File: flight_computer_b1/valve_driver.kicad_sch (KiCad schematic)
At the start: 4 parts, among them U1 IRLML6344TRPBF

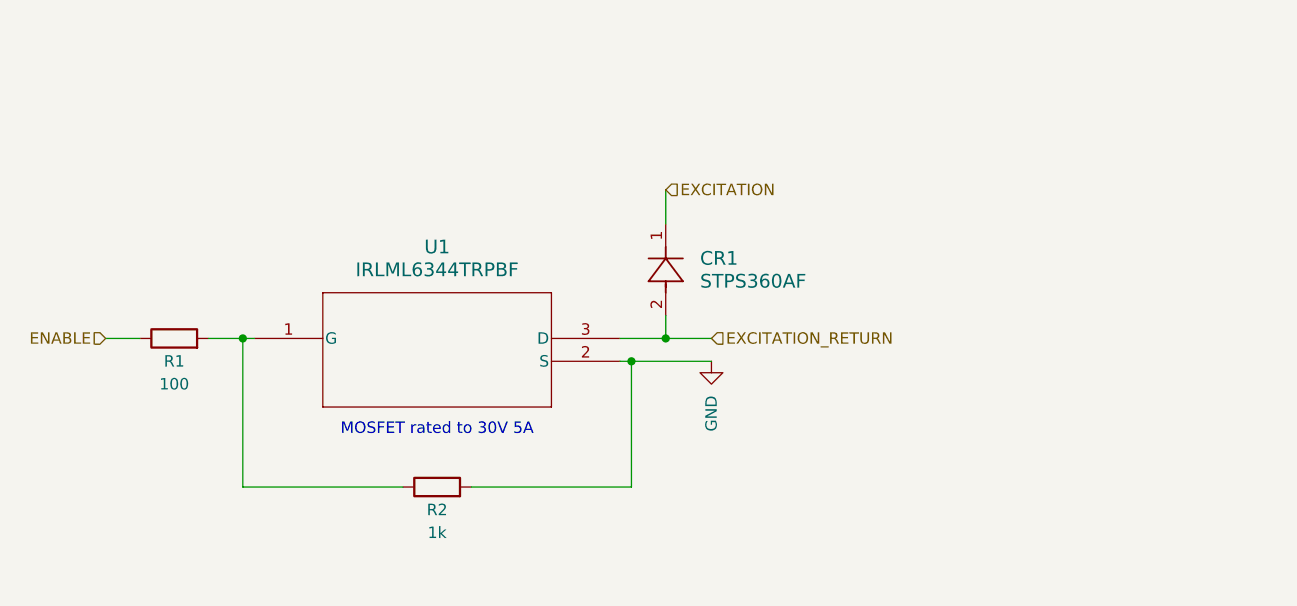
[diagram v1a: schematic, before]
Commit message: flight computer: added mux and voltage sense channels
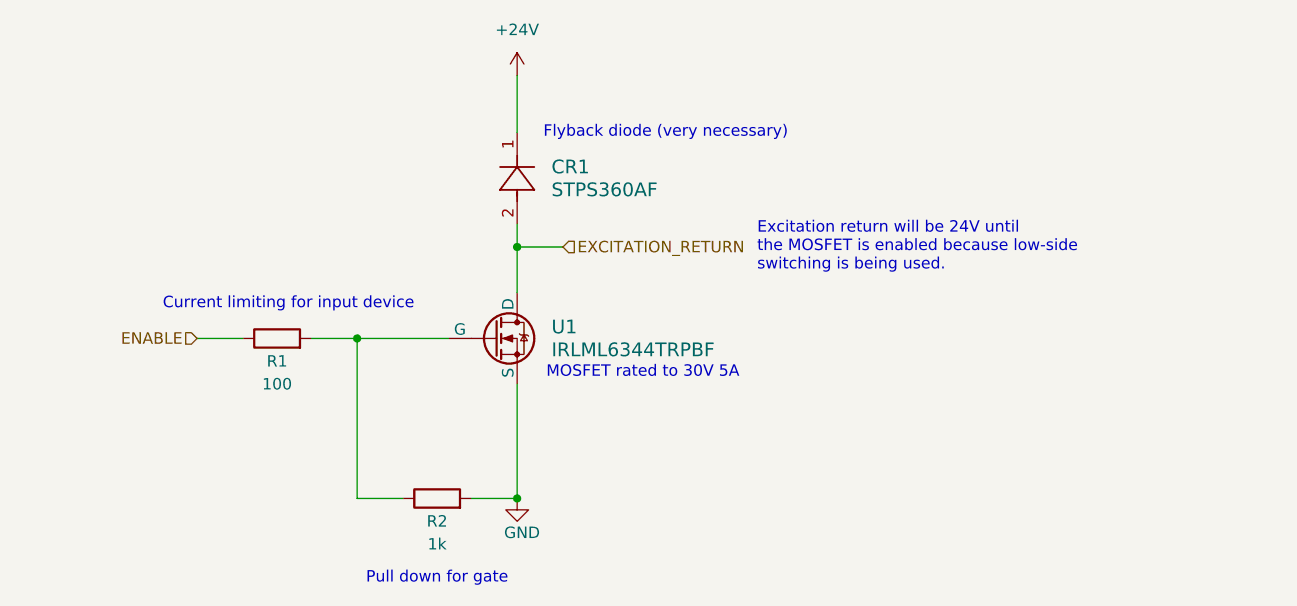
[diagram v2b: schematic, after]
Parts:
- U1: symbol IRLML6344TRPBF:IRLML6344TRPBF -> Simulation_SPICE:NMOS
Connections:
- net EXCITATION_RETURN: now also U1.1 (D); no longer U1.3 (D)
- net GND: now also U1.3 (S); no longer U1.2 (S)
- net at R1.2, R2.1: now also U1.2 (G); no longer U1.1 (G)
- net EXCITATION renamed +24V
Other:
- note added: "Current limiting for input device"
- note added: "Excitation return will be 24V until the MOSFET is enabled because low-side switching is being used."
- note added: "Flyback diode (very necessary)"
- note added: "Pull down for gate"
- company: (none) -> Purdue Space Program Liquids
- moved on the sheet: CR1, R1, R2

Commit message: flight computer: added pyro circuit and digikey part numbers
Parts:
- CR1: DIGIKEY PART N (none) -> 497-16919-1-ND
- R2: DIGIKEY PART N (none) -> YAG1237CT-ND
- U1: DIGIKEY PART N (none) -> IRLML6344TRPBFCT-ND
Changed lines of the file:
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@@
+			)
+		)
+		(property "DIGIKEY PART N" "497-16919-1-ND"
+			(at 147.32 74.93 90)
+			(effects
+				(font
+					(size 1.27 1.27)
+				)
+				(hide yes)
 			)
 		)
@@
 			)
 		)
+		(property "DIGIKEY PART N" ""
+			(at 120.65 87.63 90)
+			(effects
+				(font
+					(size 1.27 1.27)
+				)
+				(hide yes)
+			)
+		)
 		(pin "1"
 		)
@@
 		(property "Description" "Resistor"
 			(at 138.43 105.41 0)
+			(effects
+				(font
+					(size 1.27 1.27)
+				)
+				(hide yes)
+			)
+		)
+		(property "DIGIKEY PART N" "YAG1237CT-ND"
+			(at 138.43 105.41 90)
 			(effects
 				(font
@@
 			(effects
 				(font
+					(size 1.27 1.27)
+				)
+				(hide yes)
+			)
+		)
+		(property "DIGIKEY PART N" "IRLML6344TRPBFCT-ND"
+			(at 144.78 87.63 0)
+			(effects
+				(font

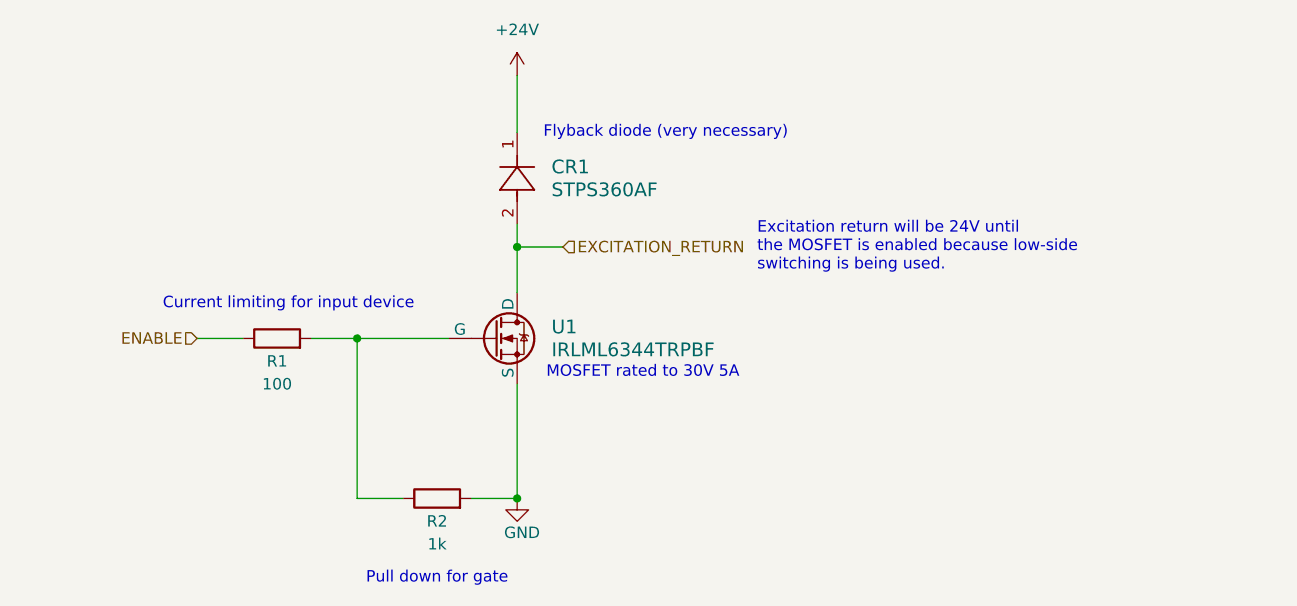
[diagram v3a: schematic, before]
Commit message: flight computer: new ideal diode, small schematic changes
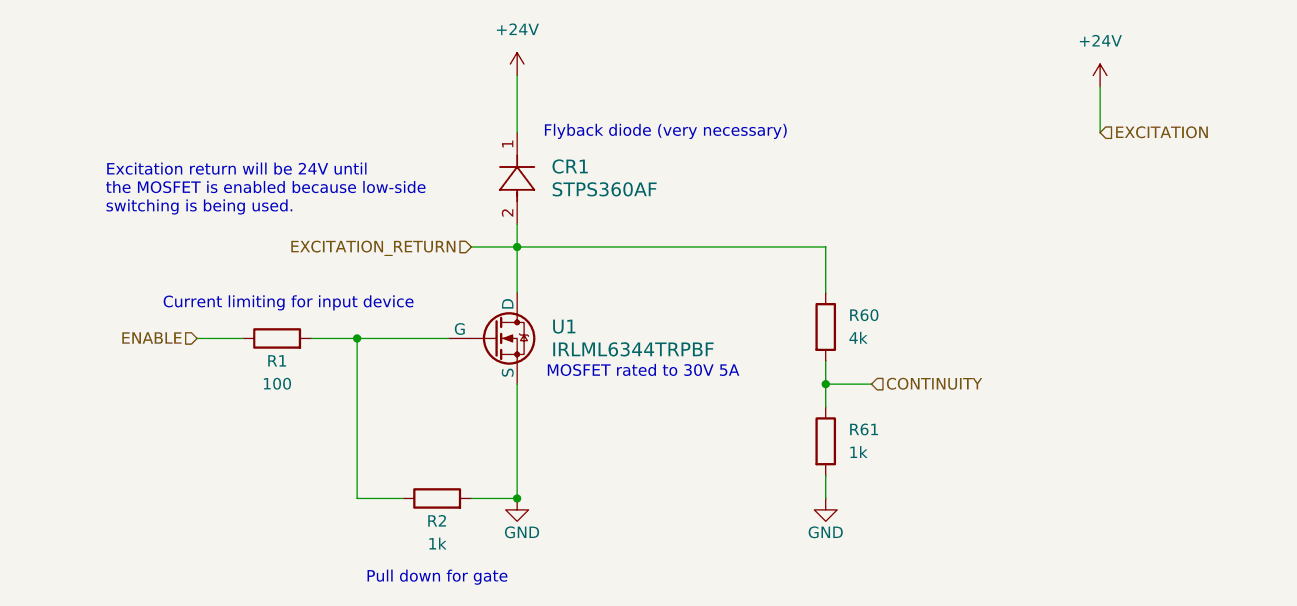
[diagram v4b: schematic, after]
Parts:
- added R60: 4k, Resistor_SMD:R_0603_1608Metric, symbol Device:R
- added R61: 1k, Resistor_SMD:R_0603_1608Metric, symbol Device:R
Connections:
- net EXCITATION_RETURN: now also R60.1
- net GND: now also R61.2
- new net CONTINUITY: R60.2, R61.1

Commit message: flight computer: routing updates
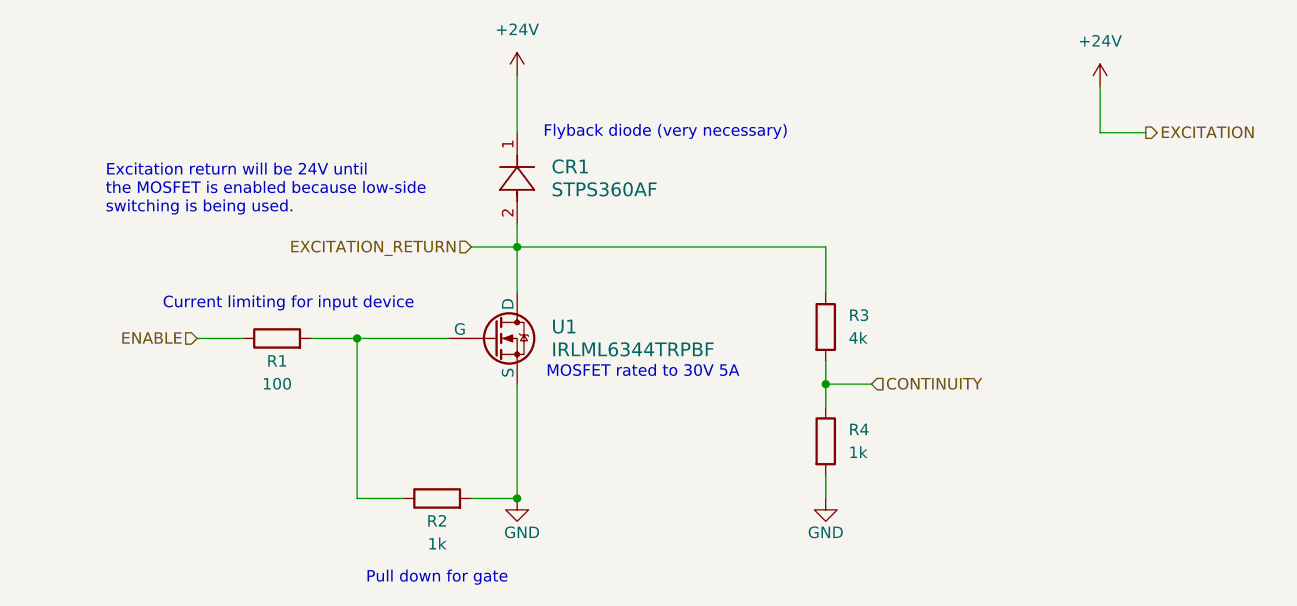
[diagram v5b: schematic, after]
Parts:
- R1: DIGIKEY PART N (none) -> 541-100HCT-ND
- renumbered R60 to R3, R61 to R4
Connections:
- net EXCITATION_RETURN: now also U1.3 (D); no longer U1.1 (D)
- net GND: now also U1.2 (S); no longer U1.3 (S)
- net at R1.2, R2.1: now also U1.1 (G); no longer U1.2 (G)
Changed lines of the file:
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@@
+	(wire
+		(pts
+			(xy 212.09 64.77) (xy 212.09 59.69)
+		)
+		(stroke
+			(width 0)
+			(type default)
+		)
+	)
 	(wire
 		(pts
@@
 	(wire
 		(pts
-			(xy 212.09 64.77) (xy 212.09 59.69)
-		)
-		(stroke
-			(width 0)
-			(type default)
-		)
-	)
-	(wire
-		(pts
 			(xy 181.61 90.17) (xy 181.61 92.71)
 		)
@@
 		(pts
 			(xy 134.62 105.41) (xy 129.54 105.41)
+		)
+		(stroke
+			(width 0)
+			(type default)
+		)
+	)
+	(wire
+		(pts
+			(xy 217.17 64.77) (xy 212.09 64.77)
 		)
 		(stroke
@@
 	)
 	(hierarchical_label "EXCITATION"
-		(shape input)
-		(at 212.09 64.77 0)
+		(shape output)
+		(at 217.17 64.77 0)
 		(effects
 			(font
@@
 			)
 		)
-		(property "DIGIKEY PART N" ""
+		(property "DIGIKEY PART N" "541-100HCT-ND"
 			(at 120.65 87.63 90)
 			(effects
@@
 			(project "flight_computer"
 				(path "/b71a7b79-cdb5-4e38-a72c-0daaa3474f05/299e6e4e-fa99-4a32-b6f8-bfb69183cdb6"
-					(reference "R7")
+					(reference "R13")
 					(unit 1)
 				)
 				(path "/b71a7b79-cdb5-4e38-a72c-0daaa3474f05/5194abae-c8be-4cd7-ad0b-bc3c23906e67"
-					(reference "R5")
+					(reference "R9")
 					(unit 1)
 				)
@@
 				)
 				(path "/b71a7b79-cdb5-4e38-a72c-0daaa3474f05/c7d93d3e-13a6-4d19-92d1-c9cec54c255f"
-					(reference "R3")
+					(reference "R5")
 					(unit 1)
 				)
@@
 		(dnp no)
 		(fields_autoplaced yes)
-		(property "Reference" "#PWR014"
+		(property "Reference" "#PWR028"
 			(at 212.09 63.5 0)
 			(effects
@@
 			(project "flight_computer"
 				(path "/b71a7b79-cdb5-4e38-a72c-0daaa3474f05/299e6e4e-fa99-4a32-b6f8-bfb69183cdb6"
-					(reference "#PWR059")
+					(reference "#PWR040")
 					(unit 1)
 				)
 				(path "/b71a7b79-cdb5-4e38-a72c-0daaa3474f05/5194abae-c8be-4cd7-ad0b-bc3c23906e67"
-					(reference "#PWR058")
+					(reference "#PWR036")
 					(unit 1)
 				)
 				(path "/b71a7b79-cdb5-4e38-a72c-0daaa3474f05/58440afa-797c-48ee-969a-78f200833b9c"
-					(reference "#PWR014")
+					(reference "#PWR028")
 					(unit 1)
 				)
 				(path "/b71a7b79-cdb5-4e38-a72c-0daaa3474f05/c7d93d3e-13a6-4d19-92d1-c9cec54c255f"
-					(reference "#PWR057")
+					(reference "#PWR032")
 					(unit 1)
 				)
@@
 			(project "flight_computer"
 				(path "/b71a7b79-cdb5-4e38-a72c-0daaa3474f05/299e6e4e-fa99-4a32-b6f8-bfb69183cdb6"
-					(reference "R8")
+					(reference "R14")
 					(unit 1)
 				)
 				(path "/b71a7b79-cdb5-4e38-a72c-0daaa3474f05/5194abae-c8be-4cd7-ad0b-bc3c23906e67"
-					(reference "R6")
+					(reference "R10")
 					(unit 1)
 				)
@@
 				)
 				(path "/b71a7b79-cdb5-4e38-a72c-0daaa3474f05/c7d93d3e-13a6-4d19-92d1-c9cec54c255f"
-					(reference "R4")
+					(reference "R6")
 					(unit 1)
 				)
@@
 		(on_board yes)
 		(dnp no)
-		(property "Reference" "#PWR01"
+		(property "Reference" "#PWR027"
 			(at 181.61 111.76 0)
 			(effects
@@
 			(project "flight_computer"
 				(path "/b71a7b79-cdb5-4e38-a72c-0daaa3474f05/299e6e4e-fa99-4a32-b6f8-bfb69183cdb6"
-					(reference "#PWR07")
+					(reference "#PWR039")
 					(unit 1)
 				)
 				(path "/b71a7b79-cdb5-4e38-a72c-0daaa3474f05/5194abae-c8be-4cd7-ad0b-bc3c23906e67"
-					(reference "#PWR06")
+					(reference "#PWR035")
 					(unit 1)
 				)
 				(path "/b71a7b79-cdb5-4e38-a72c-0daaa3474f05/58440afa-797c-48ee-969a-78f200833b9c"
-					(reference "#PWR01")
+					(reference "#PWR027")
 					(unit 1)
 				)
 				(path "/b71a7b79-cdb5-4e38-a72c-0daaa3474f05/c7d93d3e-13a6-4d19-92d1-c9cec54c255f"
-					(reference "#PWR05")
+					(reference "#PWR031")
 					(unit 1)
 				)
@@
 		(dnp no)
 		(fields_autoplaced yes)
-		(property "Reference" "R60"
+		(property "Reference" "R3"
 			(at 184.15 85.0899 0)
 			(effects
@@
 			(project "flight_computer"
 				(path "/b71a7b79-cdb5-4e38-a72c-0daaa3474f05/299e6e4e-fa99-4a32-b6f8-bfb69183cdb6"
-					(reference "R66")
+					(reference "R15")
 					(unit 1)
 				)
 				(path "/b71a7b79-cdb5-4e38-a72c-0daaa3474f05/5194abae-c8be-4cd7-ad0b-bc3c23906e67"
-					(reference "R64")
+					(reference "R11")
 					(unit 1)
 				)
 				(path "/b71a7b79-cdb5-4e38-a72c-0daaa3474f05/58440afa-797c-48ee-969a-78f200833b9c"
-					(reference "R60")
+					(reference "R3")
 					(unit 1)
 				)
 				(path "/b71a7b79-cdb5-4e38-a72c-0daaa3474f05/c7d93d3e-13a6-4d19-92d1-c9cec54c255f"
-					(reference "R62")
+					(reference "R7")
 					(unit 1)
 				)
@@
 		(dnp no)
 		(fields_autoplaced yes)
-		(property "Reference" "#PWR067"
+		(property "Reference" "#PWR025"
 			(at 147.32 62.23 0)
 			(effects
@@
 			(project ""
 				(path "/b71a7b79-cdb5-4e38-a72c-0daaa3474f05/299e6e4e-fa99-4a32-b6f8-bfb69183cdb6"
-					(reference "#PWR070")
+					(reference "#PWR037")
 					(unit 1)
 				)
 				(path "/b71a7b79-cdb5-4e38-a72c-0daaa3474f05/5194abae-c8be-4cd7-ad0b-bc3c23906e67"
-					(reference "#PWR069")
+					(reference "#PWR033")
 					(unit 1)
 				)
 				(path "/b71a7b79-cdb5-4e38-a72c-0daaa3474f05/58440afa-797c-48ee-969a-78f200833b9c"
-					(reference "#PWR067")
+					(reference "#PWR025")
 					(unit 1)
 				)
 				(path "/b71a7b79-cdb5-4e38-a72c-0daaa3474f05/c7d93d3e-13a6-4d19-92d1-c9cec54c255f"
-					(reference "#PWR068")
+					(reference "#PWR029")
 					(unit 1)
 				)
@@
 		(dnp no)
 		(fields_autoplaced yes)
-		(property "Reference" "R61"
+		(property "Reference" "R4"
 			(at 184.15 97.7899 0)
 			(effects
@@
 			(project "flight_computer"
 				(path "/b71a7b79-cdb5-4e38-a72c-0daaa3474f05/299e6e4e-fa99-4a32-b6f8-bfb69183cdb6"
-					(reference "R67")
+					(reference "R16")
 					(unit 1)
 				)
 				(path "/b71a7b79-cdb5-4e38-a72c-0daaa3474f05/5194abae-c8be-4cd7-ad0b-bc3c23906e67"
-					(reference "R65")
+					(reference "R12")
 					(unit 1)
 				)
 				(path "/b71a7b79-cdb5-4e38-a72c-0daaa3474f05/58440afa-797c-48ee-969a-78f200833b9c"
-					(reference "R61")
+					(reference "R4")
 					(unit 1)
 				)
 				(path "/b71a7b79-cdb5-4e38-a72c-0daaa3474f05/c7d93d3e-13a6-4d19-92d1-c9cec54c255f"
-					(reference "R63")
+					(reference "R8")
 					(unit 1)
 				)
@@
 			(project "flight_computer"
 				(path "/b71a7b79-cdb5-4e38-a72c-0daaa3474f05/299e6e4e-fa99-4a32-b6f8-bfb69183cdb6"
-					(reference "#PWR029")
+					(reference "#PWR038")
 					(unit 1)
 				)
 				(path "/b71a7b79-cdb5-4e38-a72c-0daaa3474f05/5194abae-c8be-4cd7-ad0b-bc3c23906e67"
-					(reference "#PWR028")
+					(reference "#PWR034")
 					(unit 1)
 				)
@@
 				)
 				(path "/b71a7b79-cdb5-4e38-a72c-0daaa3474f05/c7d93d3e-13a6-4d19-92d1-c9cec54c255f"
-					(reference "#PWR027")
-					(unit 1)
-				)
+					(reference "#PWR030")
+					(unit 1)
+				)

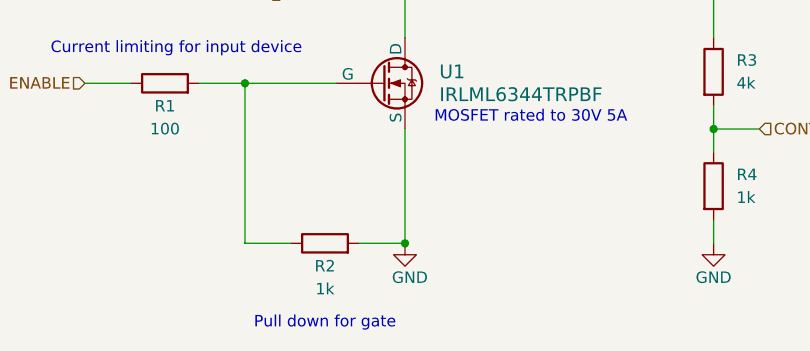
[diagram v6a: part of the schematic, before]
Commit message: routed pi traces, fixed all unavoidable DRC errors
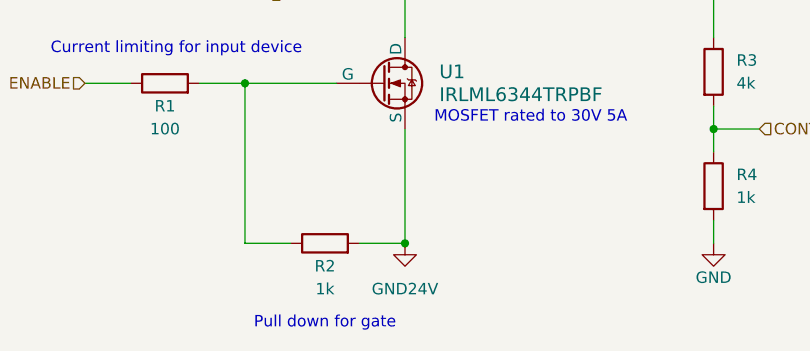
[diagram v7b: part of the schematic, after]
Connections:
- net GND: no longer R2.2, U1.2 (S)
- new net GND24V: R2.2, U1.2 (S)
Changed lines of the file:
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@@
 			)
 		)
-		(property "Value" "GND"
-			(at 149.86 109.22 0)
+		(property "Value" "GND24V"
+			(at 147.32 110.49 0)
 			(effects
 				(font
 					(size 1.27 1.27)
 				)
-				(justify right)
 			)
 		)
